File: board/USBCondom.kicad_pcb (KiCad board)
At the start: 2 copper layers, 36.1 x 19.3 mm, 8 parts

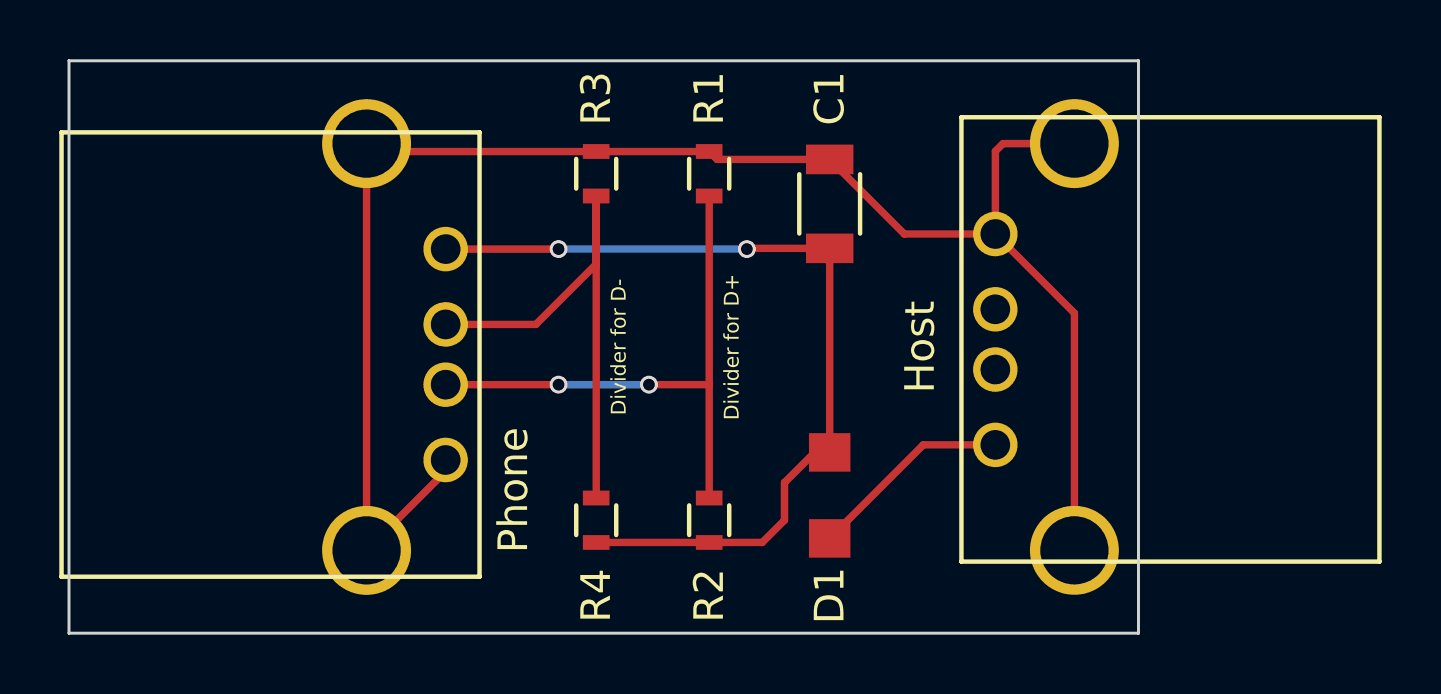
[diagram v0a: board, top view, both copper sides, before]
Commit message: Update board to rev 2
Bugfixes:
* USB shields are no longer connected to GND

Updates:
* Changed C1 footprint to 1206_HandSoldering for larger pads
* Shrank down board size and made layout more compact
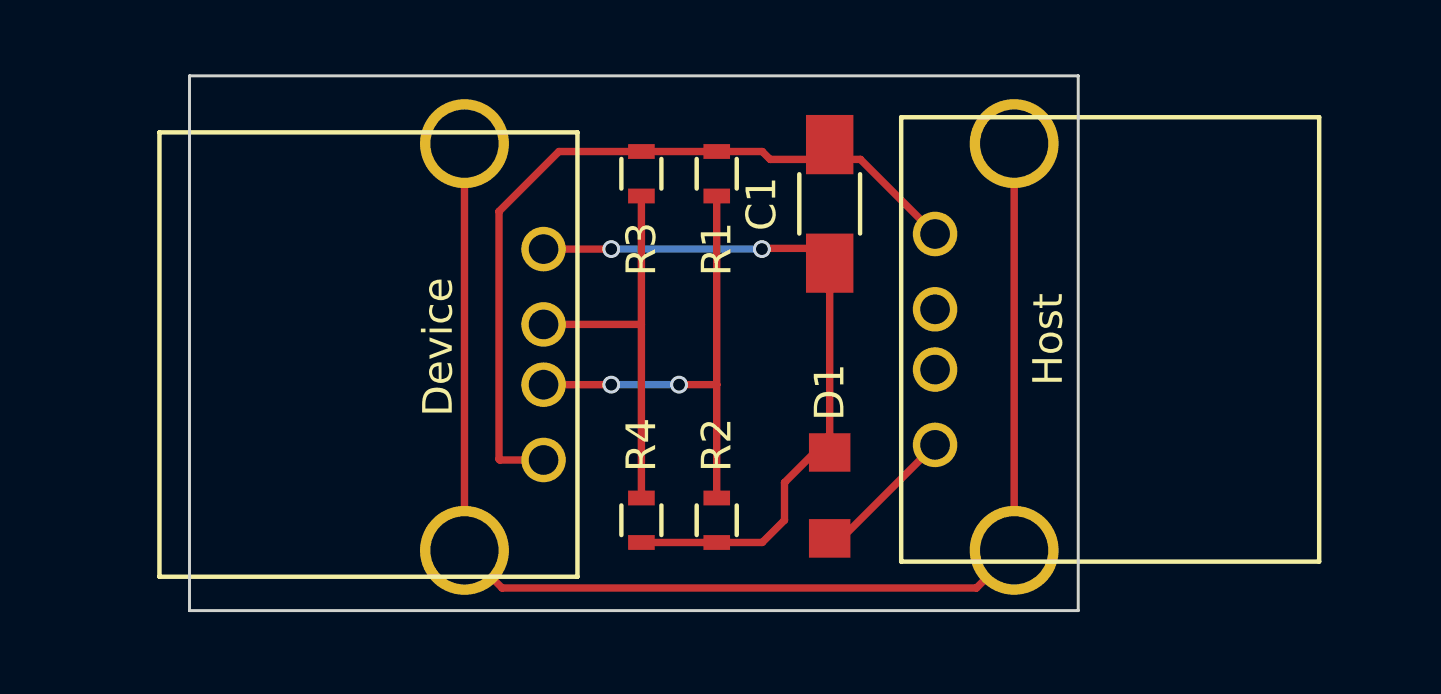
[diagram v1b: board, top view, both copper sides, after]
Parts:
- removed Host: To_Source, Connect:USB_A
- removed Phone: To_Phone, Connect:USB_A
- added ?: To_Source, Connect:USB_A, F.Cu at (172.0, 113.0)
- added ?: To_Phone, Connect:USB_A, F.Cu at (158.8, 106.4)
- C1: footprint Capacitors_SMD:C_1206 -> Capacitors_SMD:C_1206_HandSoldering
- moved R3 1.52 mm to (162.1, 103.9)
- moved R4 1.52 mm to (162.1, 115.6)
- moved R1 0.25 mm to (164.6, 103.9)
- moved R2 0.25 mm to (164.6, 115.6)
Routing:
- net /SHLD: track 0.00 -> 47.0 mm
- net /GND: track 57.7 -> 26.6 mm
- net /D-: track 18.4 -> 13.5 mm
- net /VCCphone: track 29.7 -> 25.1 mm
- net /D+: track 19.1 -> 16.0 mm
- net /VCC: track 6.89 -> 4.86 mm
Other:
- board size 36.1 x 19.3 mm -> 30 x 18 mm
- board text added: "Device"
- board text added: "Host"
- board text added: "USB condom Rev 2"
- board text removed: "Divider for D+"
- board text removed: "Divider for D-"
- board text removed: "USB condom rev 1.0"

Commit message: Update board to rev 3
Bugfixes:
* USB device side no longer has Vcc and GND swapped

Updates:
* Rounded corners on PCB
* Extended PBC to give host side port more support
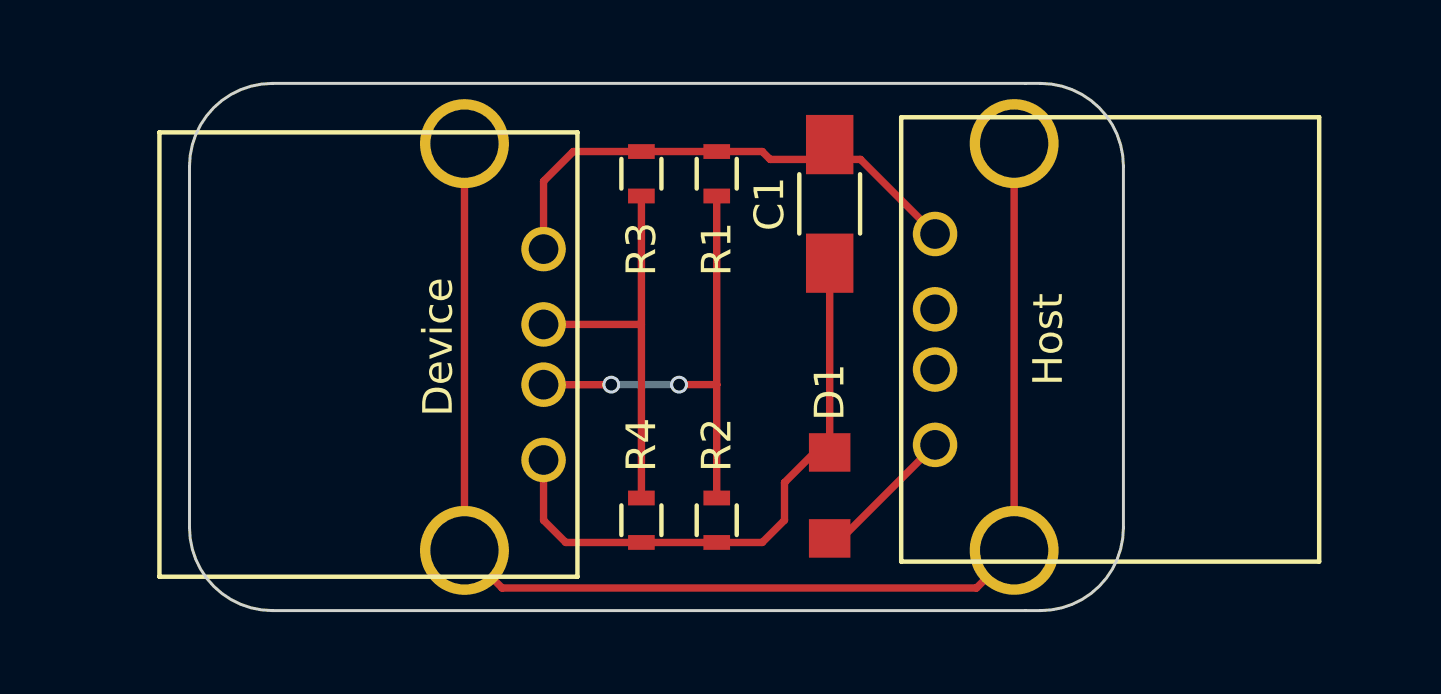
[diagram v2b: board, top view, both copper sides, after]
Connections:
- ? pad 1: /VCCphone -> /GND
- ? pad 4: /GND -> /VCCphone
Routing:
- net /GND: track 26.6 -> 17.1 mm
- net /VCCphone: track 25.1 -> 21.1 mm, vias 2 -> 0
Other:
- board size 30 x 18 mm -> 31.5 x 17.8 mm
- board text added: "USB condom Rev 3"
- board text removed: "USB condom Rev 2"
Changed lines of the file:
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@@
     (links 16)
     (no_connects 0)
-    (area 146.761999 100.533999 176.834001 118.668001)
+    (area 145.324999 100.787999 185.383001 118.668001)
     (thickness 1.6)
-    (drawings 8)
-    (tracks 43)
+    (drawings 14)
+    (tracks 37)
     (zones 0)
     (modules 8)
@@
     (34 B.Paste user)
     (35 F.Paste user)
-    (36 B.SilkS user)
+    (36 B.SilkS user hide)
     (37 F.SilkS user)
     (38 B.Mask user)
@@
     )
   )
+  (module Capacitors_SMD:C_1206_HandSoldering (layer F.Cu)
+    (at 168.402 104.902 90)
+    (descr "Capacitor SMD 1206, hand soldering")
+    (tags "capacitor 1206")
+    (attr smd)
+    (fp_text reference C1 (at 0 -2.032 90) (layer F.SilkS)
+      (effects (font (size 1 1) (thickness 0.15)))
+    )
+    (fp_text value 100uF (at 0 2.3 90) (layer F.Fab)
+      (effects (font (size 1 1) (thickness 0.15)))
+    )
+    (fp_line (start -3.3 -1.15) (end 3.3 -1.15) (layer F.CrtYd) (width 0.05))
+    (fp_line (start -3.3 1.15) (end 3.3 1.15) (layer F.CrtYd) (width 0.05))
+    (fp_line (start -3.3 -1.15) (end -3.3 1.15) (layer F.CrtYd) (width 0.05))
+    (fp_line (start 3.3 -1.15) (end 3.3 1.15) (layer F.CrtYd) (width 0.05))
+    (fp_line (start 1 -1.025) (end -1 -1.025) (layer F.SilkS) (width 0.15))
+    (fp_line (start -1 1.025) (end 1 1.025) (layer F.SilkS) (width 0.15))
+    (pad 1 smd rect (at -2 0 90) (size 2 1.6) (layers F.Cu F.Paste F.Mask)
+      (net 1 /VCCphone))
+    (pad 2 smd rect (at 2 0 90) (size 2 1.6) (layers F.Cu F.Paste F.Mask)
+      (net 2 /GND))
+    (model Capacitors_SMD.3dshapes/C_1206_HandSoldering.wrl
+      (at (xyz 0 0 0))
+      (scale (xyz 1 1 1))
+      (rotate (xyz 0 0 0))
+    )
+  )
   (module Connect:USB_A (layer F.Cu)
     (at 171.958 113.03 90)
     (descr "USB A connector")
     (tags "USB USB_A")
-    (fp_text reference "" (at 3.048 -2.286 90) (layer F.SilkS)
+    (fp_text reference "" (at 0 -2.35 90) (layer F.SilkS)
       (effects (font (size 1 1) (thickness 0.15)))
     )
@@
     (descr "USB A connector")
     (tags "USB USB_A")
-    (fp_text reference "" (at 3.556 -2.286 270) (layer F.SilkS)
+    (fp_text reference "" (at 0 -2.35 270) (layer F.SilkS)
       (effects (font (size 1 1) (thickness 0.15)))
     )
@@
     (fp_line (start 11.04986 12.95188) (end -3.93614 12.95188) (layer F.SilkS) (width 0.15))
     (pad 4 thru_hole circle (at 7.11286 -0.00212 180) (size 1.50114 1.50114) (drill 1.00076) (layers *.Cu *.Mask F.SilkS)
-      (net 2 /GND))
+      (net 1 /VCCphone))
     (pad 3 thru_hole circle (at 4.57286 -0.00212 180) (size 1.50114 1.50114) (drill 1.00076) (layers *.Cu *.Mask F.SilkS)
       (net 6 /D+))
@@
       (net 7 /D-))
     (pad 1 thru_hole circle (at 0.00086 -0.00212 180) (size 1.50114 1.50114) (drill 1.00076) (layers *.Cu *.Mask F.SilkS)
-      (net 1 /VCCphone))
+      (net 2 /GND))
     (pad 5 thru_hole circle (at 10.16086 2.66488 180) (size 2.99974 2.99974) (drill 2.30124) (layers *.Cu *.Mask F.SilkS)
       (net 8 /SHLD))
@@
     )
   )
-  (module Capacitors_SMD:C_1206_HandSoldering (layer F.Cu)
-    (at 168.402 104.902 90)
-    (descr "Capacitor SMD 1206, hand soldering")
-    (tags "capacitor 1206")
-    (attr smd)
-    (fp_text reference C1 (at 0 -2.3 90) (layer F.SilkS)
-      (effects (font (size 1 1) (thickness 0.15)))
-    )
-    (fp_text value 100uF (at 0 2.3 90) (layer F.Fab)
-      (effects (font (size 1 1) (thickness 0.15)))
-    )
-    (fp_line (start -3.3 -1.15) (end 3.3 -1.15) (layer F.CrtYd) (width 0.05))
-    (fp_line (start -3.3 1.15) (end 3.3 1.15) (layer F.CrtYd) (width 0.05))
-    (fp_line (start -3.3 -1.15) (end -3.3 1.15) (layer F.CrtYd) (width 0.05))
-    (fp_line (start 3.3 -1.15) (end 3.3 1.15) (layer F.CrtYd) (width 0.05))
-    (fp_line (start 1 -1.025) (end -1 -1.025) (layer F.SilkS) (width 0.15))
-    (fp_line (start -1 1.025) (end 1 1.025) (layer F.SilkS) (width 0.15))
-    (pad 1 smd rect (at -2 0 90) (size 2 1.6) (layers F.Cu F.Paste F.Mask)
-      (net 1 /VCCphone))
-    (pad 2 smd rect (at 2 0 90) (size 2 1.6) (layers F.Cu F.Paste F.Mask)
-      (net 2 /GND))
-    (model Capacitors_SMD.3dshapes/C_1206_HandSoldering.wrl
-      (at (xyz 0 0 0))
-      (scale (xyz 1 1 1))
-      (rotate (xyz 0 0 0))
-    )
-  )
+  (gr_line (start 175.006 118.618) (end 175.514 118.618) (angle 90) (layer Edge.Cuts) (width 0.1))
+  (gr_line (start 175.006 100.838) (end 175.514 100.838) (angle 90) (layer Edge.Cuts) (width 0.1))
+  (gr_line (start 149.606 100.838) (end 175.006 100.838) (angle 90) (layer Edge.Cuts) (width 0.1))
+  (gr_line (start 146.812 115.824) (end 146.812 103.632) (angle 90) (layer Edge.Cuts) (width 0.1))
+  (gr_line (start 175.006 118.618) (end 149.606 118.618) (angle 90) (layer Edge.Cuts) (width 0.1))
+  (gr_line (start 178.308 103.632) (end 178.308 115.824) (angle 90) (layer Edge.Cuts) (width 0.1))
+  (gr_arc (start 149.606 115.824) (end 149.606 118.618) (angle 90) (layer Edge.Cuts) (width 0.1))
+  (gr_arc (start 175.514 115.824) (end 175.514 118.618) (angle -90) (layer Edge.Cuts) (width 0.1))
+  (gr_arc (start 149.606 103.632) (end 149.606 100.838) (angle -90) (layer Edge.Cuts) (width 0.1))
+  (gr_arc (start 175.514 103.632) (end 175.514 100.838) (angle 90) (layer Edge.Cuts) (width 0.1))
   (gr_text Device (at 155.194 109.728 90) (layer F.SilkS)
     (effects (font (size 1 1) (thickness 0.15)))
@@
     (effects (font (size 1 1) (thickness 0.15)))
   )
-  (gr_line (start 146.812 100.584) (end 176.784 100.584) (angle 90) (layer Edge.Cuts) (width 0.1))
-  (gr_line (start 146.812 118.618) (end 146.812 100.584) (angle 90) (layer Edge.Cuts) (width 0.1))
-  (gr_line (start 176.784 118.618) (end 146.812 118.618) (angle 90) (layer Edge.Cuts) (width 0.1))
-  (gr_line (start 176.784 100.584) (end 176.784 118.618) (angle 90) (layer Edge.Cuts) (width 0.1))
   (gr_text "Design by\ncsammis\n\n2017" (at 151.638 109.474) (layer B.SilkS)
     (effects (font (size 1 1) (thickness 0.2)) (justify mirror))
   )
-  (gr_text "USB condom\nRev 2" (at 164.846 103.378) (layer B.SilkS)
+  (gr_text "USB condom\nRev 3" (at 164.846 103.378) (layer B.SilkS)
     (effects (font (size 1 1) (thickness 0.2)) (justify mirror))
   )
-  (segment (start 158.75212 106.42686) (end 161.03514 106.42686) (width 0.25) (layer F.Cu) (net 1))
-  (segment (start 166.14 106.402) (end 168.402 106.402) (width 0.25) (layer F.Cu) (net 1))
-  (segment (start 166.116 106.426) (end 166.14 106.402) (width 0.25) (layer F.Cu) (net 1))
-  (via (at 166.116 106.426) (size 0.6) (drill 0.4) (layers F.Cu B.Cu) (net 1))
-  (segment (start 161.036 106.426) (end 166.116 106.426) (width 0.25) (layer B.Cu) (net 1))
-  (via (at 161.036 106.426) (size 0.6) (drill 0.4) (layers F.Cu B.Cu) (net 1))
-  (segment (start 161.03514 106.42686) (end 161.036 106.426) (width 0.25) (layer F.Cu) (net 1))
+  (segment (start 162.052 116.32) (end 159.5 116.32) (width 0.25) (layer F.Cu) (net 1))
+  (segment (start 158.75212 115.57212) (end 158.75212 113.53886) (width 0.25) (layer F.Cu) (net 1))
+  (segment (start 159.5 116.32) (end 158.75212 115.57212) (width 0.25) (layer F.Cu) (net 1))
   (segment (start 162.052 116.32) (end 164.592 116.32) (width 0.25) (layer F.Cu) (net 1))
   (segment (start 168.402 113.284) (end 167.894 113.284) (width 0.25) (layer F.Cu) (net 1))
@@
   (segment (start 166.878 114.3) (end 166.878 115.57) (width 0.25) (layer F.Cu) (net 1))
   (segment (start 168.402 106.402) (end 168.402 113.284) (width 0.25) (layer F.Cu) (net 1))
-  (segment (start 162.052 103.136) (end 159.27 103.136) (width 0.25) (layer F.Cu) (net 2))
-  (segment (start 157.27486 113.53886) (end 158.75212 113.53886) (width 0.25) (layer F.Cu) (net 2))
-  (segment (start 157.25 113.514) (end 157.27486 113.53886) (width 0.25) (layer F.Cu) (net 2))
-  (segment (start 157.25 105.156) (end 157.25 113.514) (width 0.25) (layer F.Cu) (net 2))
-  (segment (start 159.27 103.136) (end 157.25 105.156) (width 0.25) (layer F.Cu) (net 2))
+  (segment (start 162.052 103.136) (end 159.754 103.136) (width 0.25) (layer F.Cu) (net 2))
+  (segment (start 158.75212 104.13788) (end 158.75212 106.42686) (width 0.25) (layer F.Cu) (net 2))
+  (segment (start 159.754 103.136) (end 158.75212 104.13788) (width 0.25) (layer F.Cu) (net 2))
+  (segment (start 169.44074 103.402) (end 171.95588 105.91714) (width 0.25) (layer F.Cu) (net 2))
   (segment (start 164.592 103.136) (end 166.128 103.136) (width 0.25) (layer F.Cu) (net 2))
   (segment (start 166.394 103.402) (end 168.402 103.402) (width 0.25) (layer F.Cu) (net 2))
@@
   (segment (start 162.052 103.136) (end 164.592 103.136) (width 0.25) (layer F.Cu) (net 2))
   (segment (start 168.402 103.402) (end 169.44074 103.402) (width 0.25) (layer F.Cu) (net 2))
-  (segment (start 169.44074 103.402) (end 171.95588 105.91714) (width 0.25) (layer F.Cu) (net 2))
   (segment (start 168.402 116.184) (end 168.80102 116.184) (width 0.25) (layer F.Cu) (net 3))
   (segment (start 168.80102 116.184) (end 171.95588 113.02914) (width 0.25) (layer F.Cu) (net 3))
@@
   (segment (start 162.052 104.636) (end 162.052 108.96686) (width 0.25) (layer F.Cu) (net 7))
   (segment (start 162.052 108.96686) (end 162.052 114.82) (width 0.25) (layer F.Cu) (net 7))
+  (segment (start 174.62288 102.86914) (end 174.62288 116.58514) (width 0.25) (layer F.Cu) (net 8))
+  (segment (start 173.35202 117.856) (end 174.62288 116.58514) (width 0.25) (layer F.Cu) (net 8))
   (segment (start 156.08512 102.87086) (end 156.08512 116.58686) (width 0.25) (layer F.Cu) (net 8))
   (segment (start 156.08512 116.58686) (end 157.35426 117.856) (width 0.25) (layer F.Cu) (net 8))
   (segment (start 157.35426 117.856) (end 173.35202 117.856) (width 0.25) (layer F.Cu) (net 8))
-  (segment (start 173.35202 117.856) (end 174.62288 116.58514) (width 0.25) (layer F.Cu) (net 8))
-  (segment (start 174.62288 102.86914) (end 174.62288 116.58514) (width 0.25) (layer F.Cu) (net 8))
 )
